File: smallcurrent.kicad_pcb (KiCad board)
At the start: 2 copper layers, 35 parts, among them J1 Screw_Terminal_01x01, J2 Screw_Terminal_01x01, J3 Screw_Terminal_01x01, J4 Screw_Terminal_01x01, J5 Conn_01x02, J6 Conn_01x04, SW1 OS203013MT8QN1-snapeda-OS2030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, SW2 OS203013MT8QN1, U1 MAX4239AUT, U2 LMV321, U3 STM809RWX6F, U4 MAX4239AUT

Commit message: Start layout
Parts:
- J3, J4: footprint homebrew:111-0703-001_BANANA_BINDING_POST -> homebrew:CT2230-BANANA-JACK
- moved J6 109.5 mm to (241.6, 81.7)
- moved C3 109.5 mm to (227.7, 112.9)
- moved R11 109.5 mm to (235.7, 112.9)
- moved R2 109.5 mm to (223.7, 112.9)
- moved C1 109.5 mm to (246.3, 102.8)
- moved C2 109.5 mm to (255.9, 85.6)
- moved C4 109.5 mm to (255.9, 83.1)
- moved C5 109.5 mm to (219.6, 112.6)
- moved C6 109.5 mm to (255.9, 80.6)
- moved D1 109.5 mm to (215.6, 112.6)
- moved J5 109.5 mm to (251.8, 92.6)
- moved R1 109.5 mm to (240.0, 104.0)
- moved R10 109.5 mm to (246.3, 105.4)
- moved R12 109.5 mm to (241.6, 107.7)
- moved R13 109.5 mm to (237.6, 107.7)
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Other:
- board outline added: 49.2 x 79.5 mm

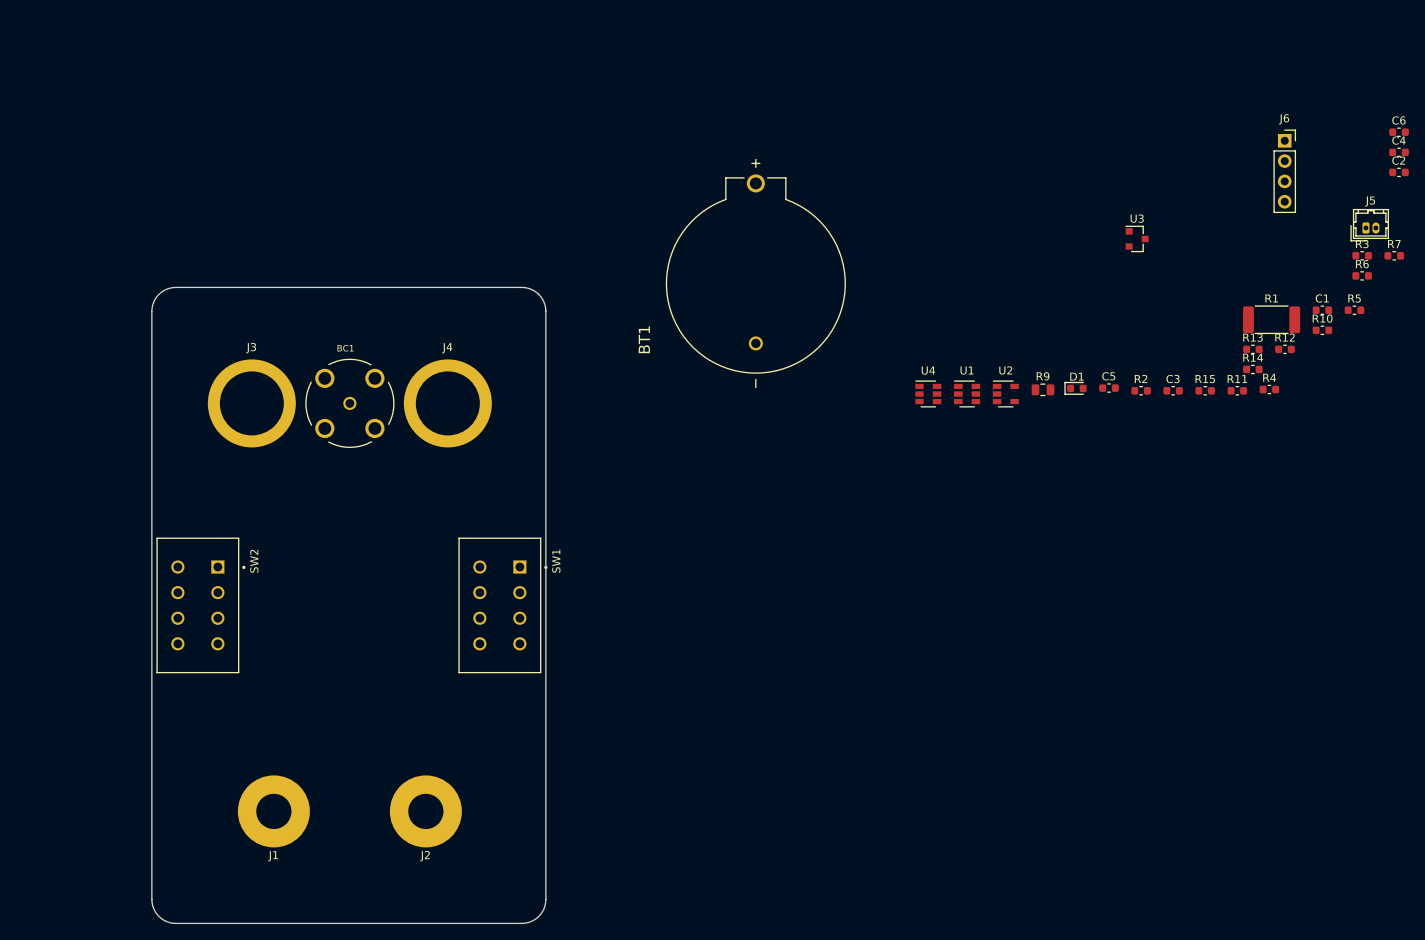
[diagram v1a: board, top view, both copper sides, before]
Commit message: More layout: most parts in position
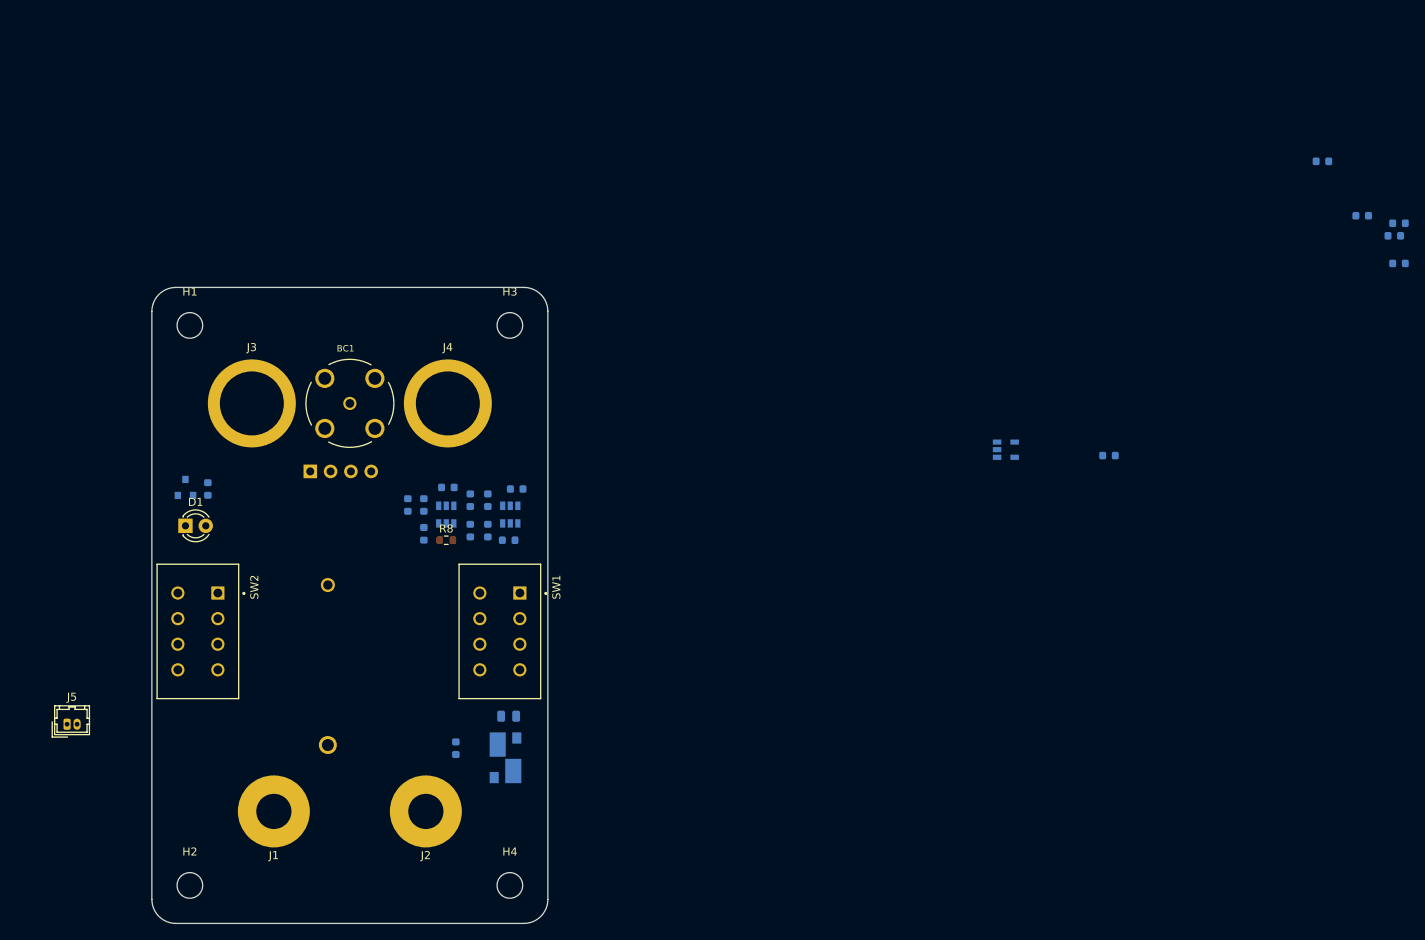
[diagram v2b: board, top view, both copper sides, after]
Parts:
- added H1: MountingHole, MountingHole:MountingHole_3.2mm_M3, F.Cu at (104.8, 104.8)
- added H2: MountingHole, MountingHole:MountingHole_3.2mm_M3, F.Cu at (104.8, 174.8)
- added H3: MountingHole, MountingHole:MountingHole_3.2mm_M3, F.Cu at (144.8, 104.8)
- added H4: MountingHole, MountingHole:MountingHole_3.2mm_M3, F.Cu at (144.8, 174.8)
- added R8: 270R, Resistor_SMD:R_0603_1608Metric, F.Cu at (136.8, 131.6)
- BT1, C1, C2, C3, C4, C5, C6, J6, R10, R11, R12, R13, R14, R15, R2, R3, R4, R5, R6, R7, R9, U1, U2, U3, U4: moved to B.Cu
- D1: footprint LED_SMD:LED_0603_1608Metric -> LED_THT:LED_D3.0mm
- R1: footprint Resistor_SMD:R_2512_6332Metric -> snapeda:Y14870R01000B9R; moved to B.Cu
- moved J5 173.8 mm to (89.4, 154.6)
- moved R4 133.3 mm to (107.0, 125.2), turned to 90 degrees
- moved C4 131.5 mm to (132.0, 127.2), turned to 270 degrees
- moved J6 128.6 mm to (119.8, 123.0), turned to 270 degrees
- moved U3 122.9 mm to (104.2, 125.0), turned to 90 degrees
- moved R3 113.5 mm to (142.0, 126.6), turned to 90 degrees
- moved R5 113.1 mm to (139.8, 126.6), turned to 90 degrees
- moved D1 112.7 mm to (104.2, 129.8)
- moved R1 110.3 mm to (144.2, 158.8), turned to 90 degrees
- moved R14 105.6 mm to (134.0, 130.8), turned to 90 degrees
- moved R13 105.4 mm to (134.0, 127.2), turned to 90 degrees
- moved C1 103.2 mm to (145.6, 125.2)
- moved R12 99.9 mm to (144.6, 131.6)
- moved R2 96.6 mm to (138.0, 157.6), turned to 270 degrees
- moved R15 95.4 mm to (137.0, 125.0)
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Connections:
- C4 pad 2: Net-(BC1-Pad1) -> Net-(C4-Pad2)
- J2 pad 1: Net-(J2-Pad1) -> GNDREF
- R1 pad 2: Net-(J2-Pad1) -> GNDREF
- R14 pad 1: Net-(BC1-Pad1) -> Net-(C4-Pad2)
- R2 pad 2: Net-(J2-Pad1) -> GNDREF
- SW2 pad 4: Net-(J2-Pad1) -> GNDREF
- U4 pad 1: Net-(BC1-Pad1) -> Net-(C4-Pad2)
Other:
- board size 49.2 x 79.5 mm -> 49.5 x 79.5 mm

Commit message: Version 1.0
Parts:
- added G***: OSHW_LOGO_4mm, homebrew:OSHW_LOGO_4mm, F.Cu at (104.8, 168.2)
- J5, R8: moved to B.Cu
- moved R7 137.1 mm to (122.6, 128.0), turned to 90 degrees
- moved R6 134.8 mm to (122.6, 131.0), turned to 90 degrees
- moved C6 133.8 mm to (125.4, 126.6), turned to 90 degrees
- moved C2 131.3 mm to (129.0, 125.8)
- moved R10 125.5 mm to (128.8, 128.4), turned to 270 degrees
- moved C5 87.9 mm to (131.8, 123.8)
- moved U2 82.2 mm to (125.2, 130.4), turned to 270 degrees
- moved J5 34.3 mm to (111.8, 128.6)
- moved J6 7.24 mm to (112.6, 123.8)
- turned J4 to 270 degrees
- turned R1 to 270 degrees
- turned R12 to 180 degrees
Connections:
- BC1 pad 3: (no net) -> GNDREF
- BC1 pad 4: (no net) -> GNDREF
- BC1 pad 5: (no net) -> GNDREF
- C4 pad 2: Net-(C4-Pad2) -> Net-(BC1-Pad1)
- R14 pad 1: Net-(C4-Pad2) -> Net-(BC1-Pad1)
- R8 pad 2: Net-(C4-Pad2) -> Net-(R8-Pad2)
- U3 pad 1: VCC -> GND
- U3 pad 3: GND -> VCC
- U4 pad 1: Net-(C4-Pad2) -> Net-(R8-Pad2)
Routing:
- net GNDREF: track 0.00 -> 192.8 mm
- net Net-(J1-Pad1): track 0.00 -> 128.8 mm
- net VCC: track 0.00 -> 87.5 mm, vias 0 -> 2
- net GND: track 0.00 -> 83.2 mm, vias 0 -> 4
- net Net-(BC1-Pad1): track 0.00 -> 52.4 mm
- net +BATT: track 0.00 -> 49.7 mm
- net Net-(R9-Pad1): track 0.00 -> 24.3 mm
- net Net-(R12-Pad1): track 0.00 -> 18.6 mm
- net Net-(R1-Pad1): track 0.00 -> 16.0 mm
- net Net-(C3-Pad2): track 0.00 -> 15.0 mm
- net Net-(J6-Pad4): track 0.00 -> 9.26 mm
- net Net-(C3-Pad1): track 0.00 -> 8.04 mm
- net Net-(C4-Pad1): track 0.00 -> 6.67 mm
- net Net-(R10-Pad2): track 0.00 -> 4.90 mm
- net Net-(R4-Pad2): track 0.00 -> 4.41 mm
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- added copper zone on F.Cu, net GNDREF
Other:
- rule pad_to_mask_clearance: 0.05 -> 0
- board text added: "+"
- board text added: "-"
- board text added: "1 mV/mA 10m"
- board text added: "1 mV/nA 10k"
- board text added: "1mV/μA 10R"
- board text added: "5.5v max"
- board text added: "BATT OK"
- board text added: "CR2032"
- board text added: "Current Input"
- board text added: "OFF"
- board text added: "ON"
- board text added: "R7"
- board text added: "SHORT"
- board text added: "Voltage Output"
- board text added: "smallCurrent v1.0"
